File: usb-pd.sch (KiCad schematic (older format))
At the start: 32 parts, among them J12 12401598E4_2A, Q7 SQS401EN-T1_BE3, U18 STUSB4500QTR

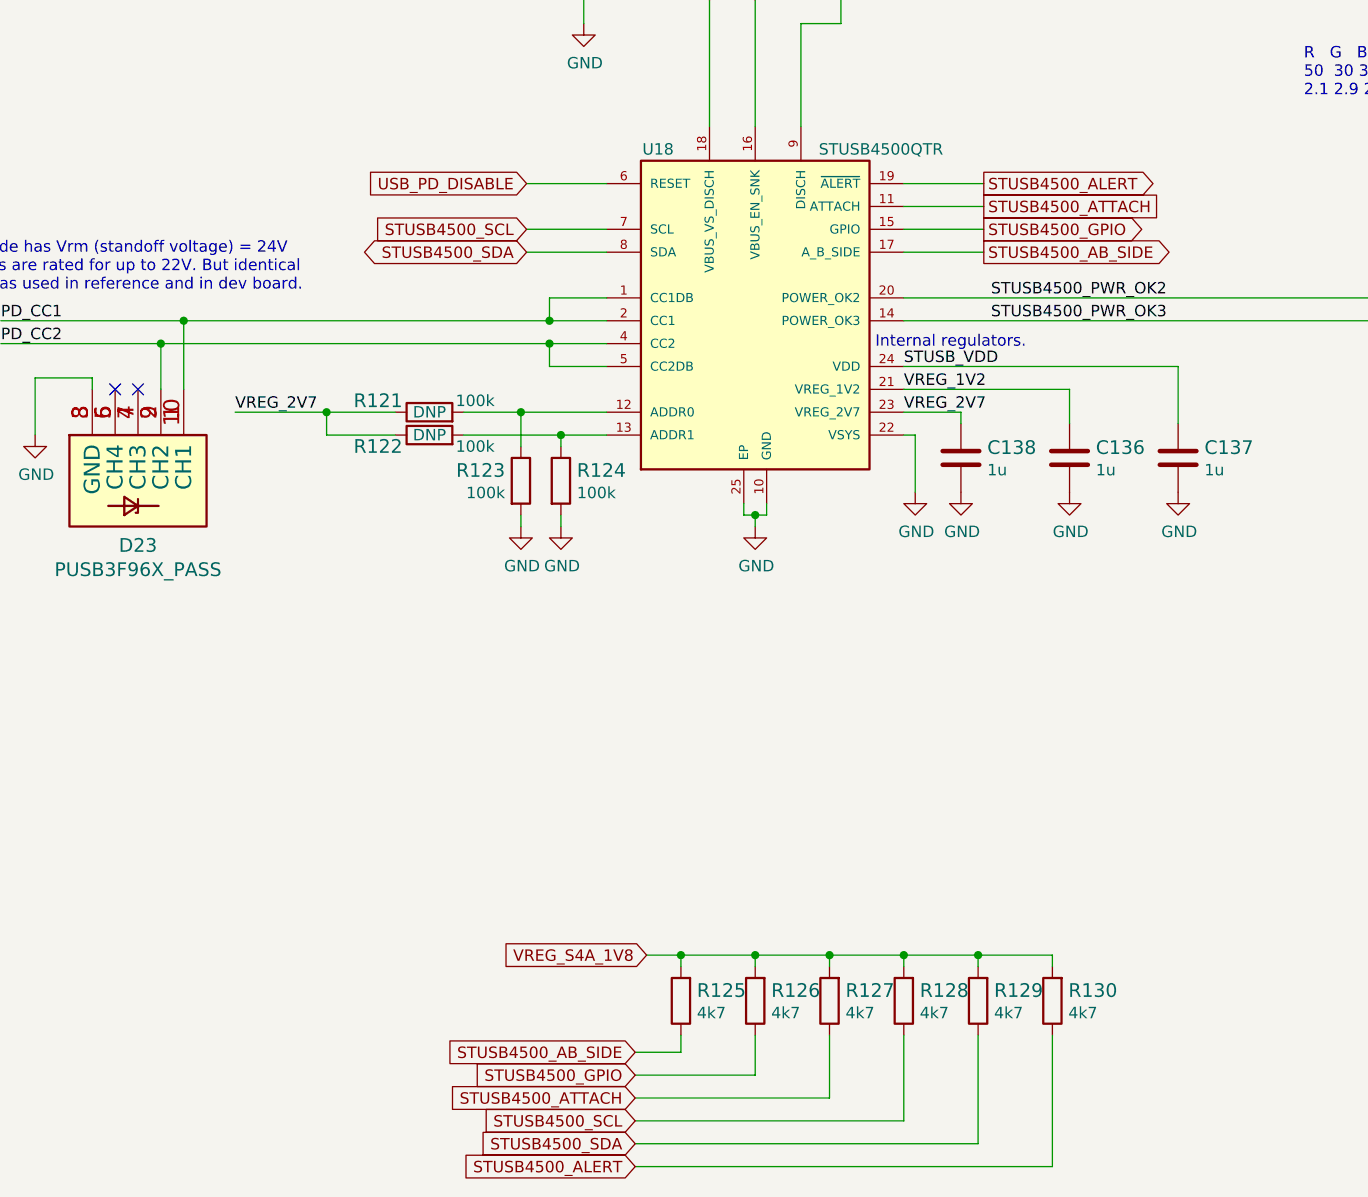
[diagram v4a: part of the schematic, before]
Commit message: Connect STUSB4500 signals to SoM
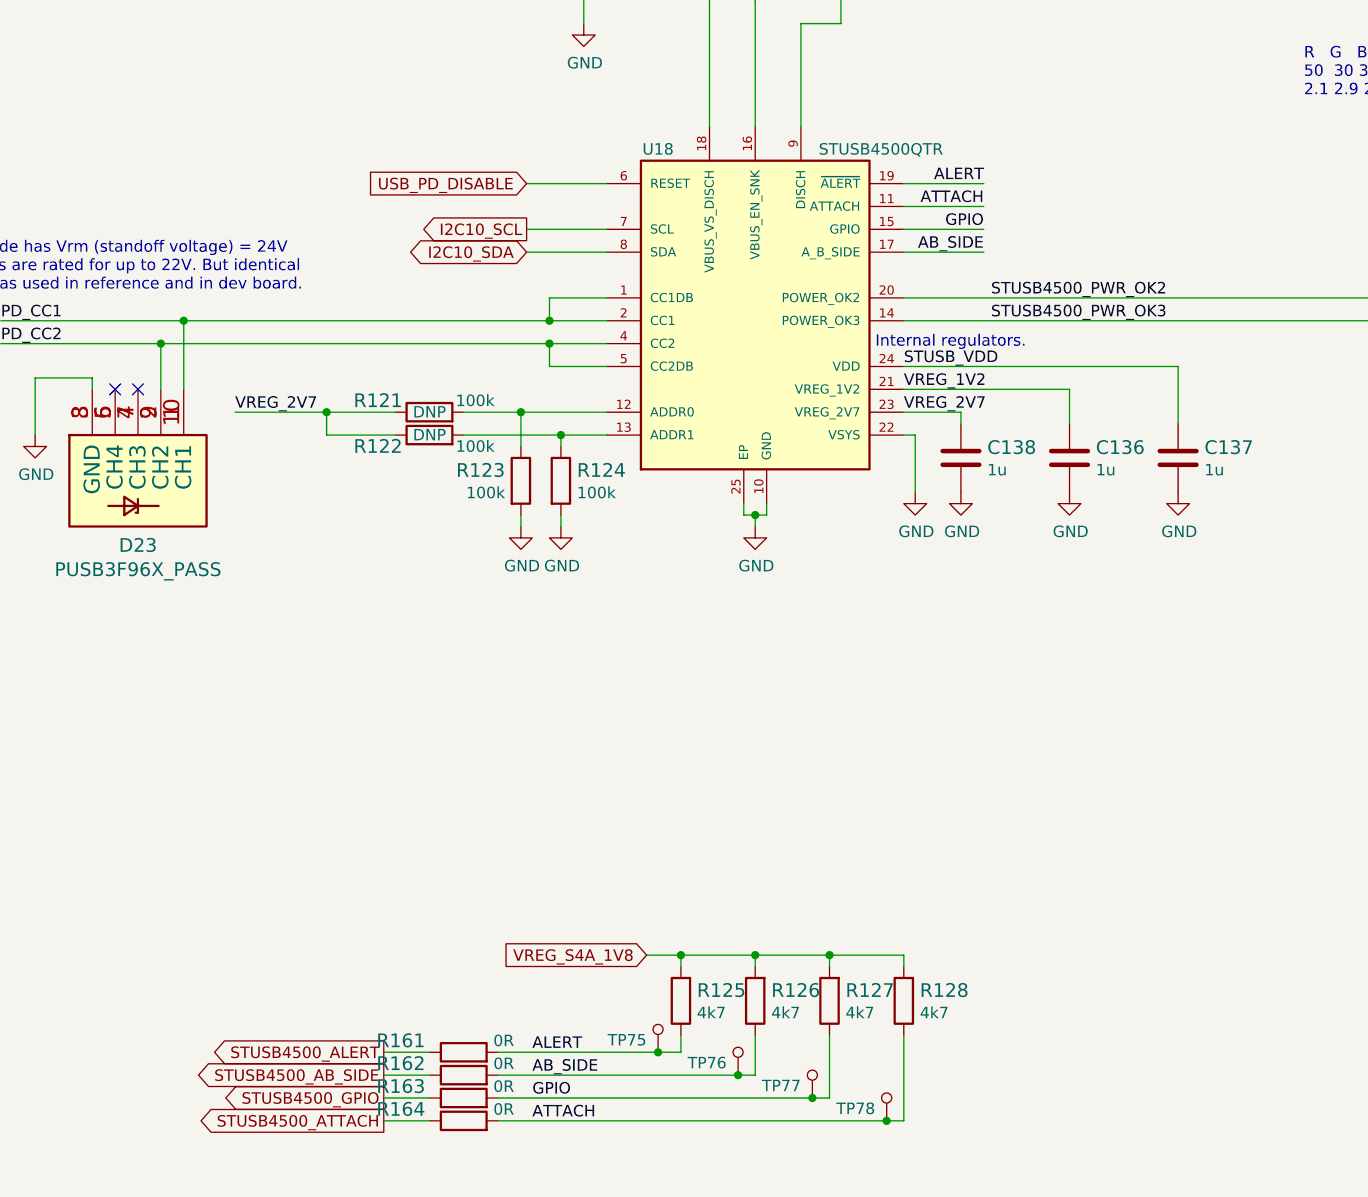
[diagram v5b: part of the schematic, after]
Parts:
- removed R129, R130: R_4k7_0402, sa800u-baseboard-hw-footprints:0402-res, symbol sa800u-baseboard-hw:R_4k7_0402
- added R161, R162, R163, R164: R_0R_0402, sa800u-baseboard-hw-footprints:0402-res, symbol sa800u-baseboard-hw:R_0R_0402
- added TP75, TP76, TP77, TP78: TP_SMD_0_75MM, sa800u-baseboard-hw-footprints:Testpoint_smd_0_75mm, symbol sa800u-baseboard-hw:TP_SMD_0_75MM
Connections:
- net STUSB4500_AB_SIDE: now also R162.1; no longer R125.1, U18.17 (A_B_SIDE)
- net STUSB4500_ALERT: now also R161.1; no longer U18.19 (~ALERT)
- net STUSB4500_ATTACH: now also R164.1; no longer R127.1, U18.11 (ATTACH)
- net STUSB4500_GPIO: now also R163.1; no longer R126.1, U18.15 (GPIO)
- net STUSB4500_SCL renamed ATTACH
- net ATTACH: now also U18.11 (ATTACH), R164.2, TP78.1; no longer U18.7 (SCL)
- net STUSB4500_SDA renamed I2C10_SDA
- new net AB_SIDE: R126.1, R162.2, TP76.1, U18.17 (A_B_SIDE)
- new net ALERT: R125.1, R161.2, TP75.1, U18.19 (~ALERT)
- new net GPIO: R127.1, R163.2, TP77.1, U18.15 (GPIO)
- new net I2C10_SCL: U18.7 (SCL)
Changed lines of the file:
@@
 	1    0    0    -1
 $EndComp
-Text GLabel 6350 4000 0    50   BiDi ~ 0
-STUSB4500_SDA
-Text GLabel 6350 3900 0    50   Input ~ 0
-STUSB4500_SCL
 Wire Wire Line
 	6350 3900 6700 3900
 Wire Wire Line
 	6350 4000 6700 4000
-Text GLabel 6825 7900 0    50   Input ~ 0
-STUSB4500_SDA
-Text GLabel 6825 7800 0    50   Input ~ 0
-STUSB4500_SCL
-Text GLabel 8350 3700 2    50   Output ~ 0
+Wire Wire Line
+	8000 3700 8350 3700
+Text GLabel 5725 7500 0    50   Output ~ 0
 STUSB4500_ALERT
 Wire Wire Line
-	8000 3700 8350 3700
-Text GLabel 6825 8000 0    50   Input ~ 0
-STUSB4500_ALERT
-Wire Wire Line
 	8000 3800 8350 3800
-Text GLabel 8350 3800 2    50   UnSpc ~ 0
+Wire Wire Line
+	8000 3900 8350 3900
+Wire Wire Line
+	8350 4000 8000 4000
+Text GLabel 5725 7800 0    50   Output ~ 0
 STUSB4500_ATTACH
-Text GLabel 8350 3900 2    50   Output ~ 0
+Text GLabel 5725 7700 0    50   Output ~ 0
 STUSB4500_GPIO
-Wire Wire Line
-	8000 3900 8350 3900
-Text GLabel 8350 4000 2    50   Output ~ 0
-STUSB4500_AB_SIDE
-Wire Wire Line
-	8350 4000 8000 4000
-Text GLabel 6825 7700 0    50   Input ~ 0
-STUSB4500_ATTACH
-Text GLabel 6825 7600 0    50   Input ~ 0
-STUSB4500_GPIO
-Text GLabel 6825 7500 0    50   Input ~ 0
+Text GLabel 5725 7600 0    50   Output ~ 0
 STUSB4500_AB_SIDE
 Wire Wire Line
@@
 	7025 7500 7025 7425
 Wire Wire Line
-	6825 7500 7025 7500
-Wire Wire Line
 	7350 7600 7350 7425
 Wire Wire Line
-	6825 7600 7350 7600
+	6225 7600 7275 7600
 Wire Wire Line
 	7675 7700 7675 7425
 Wire Wire Line
-	6825 7700 7675 7700
+	6225 7700 7600 7700
 $Comp
 L sa800u-baseboard-hw:R_4k7_0402 R128
@@
 	0    -1   -1   0
 $EndComp
-$Comp
-L sa800u-baseboard-hw:R_4k7_0402 R129
-U 1 1 62F55A6F
-P 8325 7275
-F 0 "R129" V 8370 7205 60  0000 R CNN
-F 1 "R_4k7_0402" H 8325 7125 60  0001 C CNN
-F 2 "sa800u-baseboard-hw-footprints:0402-res" H 8525 7475 60  0001 L CNN
-F 3 "" H 8325 7275 50  0001 C CNN
-F 4 "VISHAY" H 8525 7675 60  0001 L CNN "Manufacturer"
-F 5 "MCS04020C4701FE000" H 8525 7575 60  0001 L CNN "MPN"
-F 6 "4k7" V 8272 7205 50  0000 R CNN "Val"
-	1    8325 7275
-	0    -1   -1   0
-$EndComp
 Wire Wire Line
 	7675 7075 8000 7075
@@
 	8000 7075 8000 7125
 Wire Wire Line
-	8000 7075 8325 7075
-Wire Wire Line
-	8325 7075 8325 7125
-Connection ~ 8000 7075
-$Comp
-L sa800u-baseboard-hw:R_4k7_0402 R130
-U 1 1 62F5B4FE
-P 8650 7275
-F 0 "R130" V 8695 7205 60  0000 R CNN
-F 1 "R_4k7_0402" H 8650 7125 60  0001 C CNN
-F 2 "sa800u-baseboard-hw-footprints:0402-res" H 8850 7475 60  0001 L CNN
-F 3 "" H 8650 7275 50  0001 C CNN
-F 4 "VISHAY" H 8850 7675 60  0001 L CNN "Manufacturer"
-F 5 "MCS04020C4701FE000" H 8850 7575 60  0001 L CNN "MPN"
-F 6 "4k7" V 8597 7205 50  0000 R CNN "Val"
-	1    8650 7275
-	0    -1   -1   0
-$EndComp
-Wire Wire Line
-	8325 7075 8650 7075
-Wire Wire Line
-	8650 7075 8650 7125
-Wire Wire Line
 	8000 7800 8000 7425
 Wire Wire Line
-	6825 7800 8000 7800
-Wire Wire Line
-	8325 7900 8325 7425
-Wire Wire Line
-	6825 7900 8325 7900
-Wire Wire Line
-	8650 8000 8650 7425
-Wire Wire Line
-	6825 8000 8650 8000
+	6225 7800 7925 7800
 Connection ~ 7675 7075
-Connection ~ 8325 7075
 Wire Wire Line
 	7150 2900 7150 3450
@@
 Text Label 5075 4700 0    50   ~ 0
 VREG_2V7
+$Comp
+L sa800u-baseboard-hw:TP_SMD_0_75MM TP?
+U 1 1 620ECAFB
+P 6925 7400
+AR Path="/61B0DC30/620ECAFB" Ref="TP?"  Part="1"
+AR Path="/61DF77CE/620ECAFB" Ref="TP75"  Part="1"
+F 0 "TP75" H 6975 7447 50  0000 L CNN
+F 1 "TP_SMD_0_75MM" H 6925 7300 50  0001 C CNN
+F 2 "sa800u-baseboard-hw-footprints:Testpoint_smd_0_75mm" H 7125 7600 60  0001 L CNN
+F 3 "" H 7125 7700 60  0001 L CNN
+	1    6925 7400
+	-1   0    0    1
+$EndComp
+$Comp
+L sa800u-baseboard-hw:TP_SMD_0_75MM TP?
+U 1 1 6211F056
+P 7275 7500
+AR Path="/61B0DC30/6211F056" Ref="TP?"  Part="1"
+AR Path="/61DF77CE/6211F056" Ref="TP76"  Part="1"
+F 0 "TP76" H 7325 7547 50  0000 L CNN
+F 1 "TP_SMD_0_75MM" H 7275 7400 50  0001 C CNN
+F 2 "sa800u-baseboard-hw-footprints:Testpoint_smd_0_75mm" H 7475 7700 60  0001 L CNN
+F 3 "" H 7475 7800 60  0001 L CNN
+	1    7275 7500
+	-1   0    0    1
+$EndComp
+$Comp
+L sa800u-baseboard-hw:TP_SMD_0_75MM TP?
+U 1 1 62123DE3
+P 7600 7600
+AR Path="/61B0DC30/62123DE3" Ref="TP?"  Part="1"
+AR Path="/61DF77CE/62123DE3" Ref="TP77"  Part="1"
+F 0 "TP77" H 7650 7647 50  0000 L CNN
+F 1 "TP_SMD_0_75MM" H 7600 7500 50  0001 C CNN
+F 2 "sa800u-baseboard-hw-footprints:Testpoint_smd_0_75mm" H 7800 7800 60  0001 L CNN
+F 3 "" H 7800 7900 60  0001 L CNN
+	1    7600 7600
+	-1   0    0    1
+$EndComp
+$Comp
+L sa800u-baseboard-hw:TP_SMD_0_75MM TP?
+U 1 1 6212893D
+P 7925 7700
+AR Path="/61B0DC30/6212893D" Ref="TP?"  Part="1"
+AR Path="/61DF77CE/6212893D" Ref="TP78"  Part="1"
+F 0 "TP78" H 7975 7747 50  0000 L CNN
+F 1 "TP_SMD_0_75MM" H 7925 7600 50  0001 C CNN
+F 2 "sa800u-baseboard-hw-footprints:Testpoint_smd_0_75mm" H 8125 7900 60  0001 L CNN
+F 3 "" H 8125 8000 60  0001 L CNN
+	1    7925 7700
+	-1   0    0    1
+$EndComp
+Connection ~ 7925 7800
+Wire Wire Line
+	7925 7800 8000 7800
+Connection ~ 7600 7700
+Wire Wire Line
+	7600 7700 7675 7700
+Connection ~ 7275 7600
+Wire Wire Line
+	7275 7600 7350 7600
+Connection ~ 6925 7500
+Wire Wire Line
+	6925 7500 7025 7500
+Wire Wire Line
+	6225 7500 6925 7500
+$Comp
+L sa800u-baseboard-hw:R_0R_0402 R?
+U 1 1 62272ADE
+P 6075 7600
+AR Path="/61C01D88/62272ADE" Ref="R?"  Part="1"
+AR Path="/61DF77CE/62272ADE" Ref="R162"  Part="1"
+F 0 "R162" H 5800 7650 60  0000 C CNN
+F 1 "R_0R_0402" H 6075 7450 60  0001 C CNN
+F 2 "sa800u-baseboard-hw-footprints:0402-res" H 6275 7800 60  0001 L CNN
+F 3 "" H 6075 7600 50  0001 C CNN
+F 4 "PANASONIC" H 6275 8000 60  0001 L CNN "Manufacturer"
+F 5 "ERJ2GE0R00X" H 6275 7900 60  0001 L CNN "MPN"
+F 6 "0R" H 6250 7650 50  0000 C CNN "Val"
+	1    6075 7600
+	1    0    0    -1
+$EndComp
+$Comp
+L sa800u-baseboard-hw:R_0R_0402 R?
+U 1 1 6228B532
+P 6075 7500
+AR Path="/61C01D88/6228B532" Ref="R?"  Part="1"
+AR Path="/61DF77CE/6228B532" Ref="R161"  Part="1"
+F 0 "R161" H 5800 7550 60  0000 C CNN
+F 1 "R_0R_0402" H 6075 7350 60  0001 C CNN
+F 2 "sa800u-baseboard-hw-footprints:0402-res" H 6275 7700 60  0001 L CNN
+F 3 "" H 6075 7500 50  0001 C CNN
+F 4 "PANASONIC" H 6275 7900 60  0001 L CNN "Manufacturer"
+F 5 "ERJ2GE0R00X" H 6275 7800 60  0001 L CNN "MPN"
+F 6 "0R" H 6250 7550 50  0000 C CNN "Val"
+	1    6075 7500
+	1    0    0    -1
+$EndComp
+$Comp
+L sa800u-baseboard-hw:R_0R_0402 R?
+U 1 1 622914DD
+P 6075 7800
+AR Path="/61C01D88/622914DD" Ref="R?"  Part="1"
+AR Path="/61DF77CE/622914DD" Ref="R164"  Part="1"
+F 0 "R164" H 5800 7850 60  0000 C CNN
+F 1 "R_0R_0402" H 6075 7650 60  0001 C CNN
+F 2 "sa800u-baseboard-hw-footprints:0402-res" H 6275 8000 60  0001 L CNN
+F 3 "" H 6075 7800 50  0001 C CNN
+F 4 "PANASONIC" H 6275 8200 60  0001 L CNN "Manufacturer"
+F 5 "ERJ2GE0R00X" H 6275 8100 60  0001 L CNN "MPN"
+F 6 "0R" H 6250 7850 50  0000 C CNN "Val"
+	1    6075 7800
+	1    0    0    -1
+$EndComp
+$Comp
+L sa800u-baseboard-hw:R_0R_0402 R?
+U 1 1 622914E6
+P 6075 7700
+AR Path="/61C01D88/622914E6" Ref="R?"  Part="1"
+AR Path="/61DF77CE/622914E6" Ref="R163"  Part="1"
+F 0 "R163" H 5800 7750 60  0000 C CNN
+F 1 "R_0R_0402" H 6075 7550 60  0001 C CNN
+F 2 "sa800u-baseboard-hw-footprints:0402-res" H 6275 7900 60  0001 L CNN
+F 3 "" H 6075 7700 50  0001 C CNN
+F 4 "PANASONIC" H 6275 8100 60  0001 L CNN "Manufacturer"
+F 5 "ERJ2GE0R00X" H 6275 8000 60  0001 L CNN "MPN"
+F 6 "0R" H 6250 7750 50  0000 C CNN "Val"
+	1    6075 7700
+	1    0    0    -1
+$EndComp
+Wire Wire Line
+	5925 7500 5725 7500
+Wire Wire Line
+	5925 7600 5725 7600
+Wire Wire Line
+	5925 7700 5725 7700
+Wire Wire Line
+	5925 7800 5725 7800
+Text Label 6375 7500 0    50   ~ 0
+ALERT
+Text Label 6375 7600 0    50   ~ 0
+AB_SIDE
+Text Label 6375 7700 0    50   ~ 0
+GPIO
+Text Label 6375 7800 0    50   ~ 0
+ATTACH
+Text Label 8350 3700 2    50   ~ 0
+ALERT
+Text Label 8350 4000 2    50   ~ 0
+AB_SIDE
+Text Label 8350 3900 2    50   ~ 0
+GPIO
+Text Label 8350 3800 2    50   ~ 0
+ATTACH
+Text GLabel 6350 3900 0    50   Output ~ 0
+I2C10_SCL
+Text GLabel 6350 4000 0    50   BiDi ~ 0
+I2C10_SDA
 $EndSCHEMATC

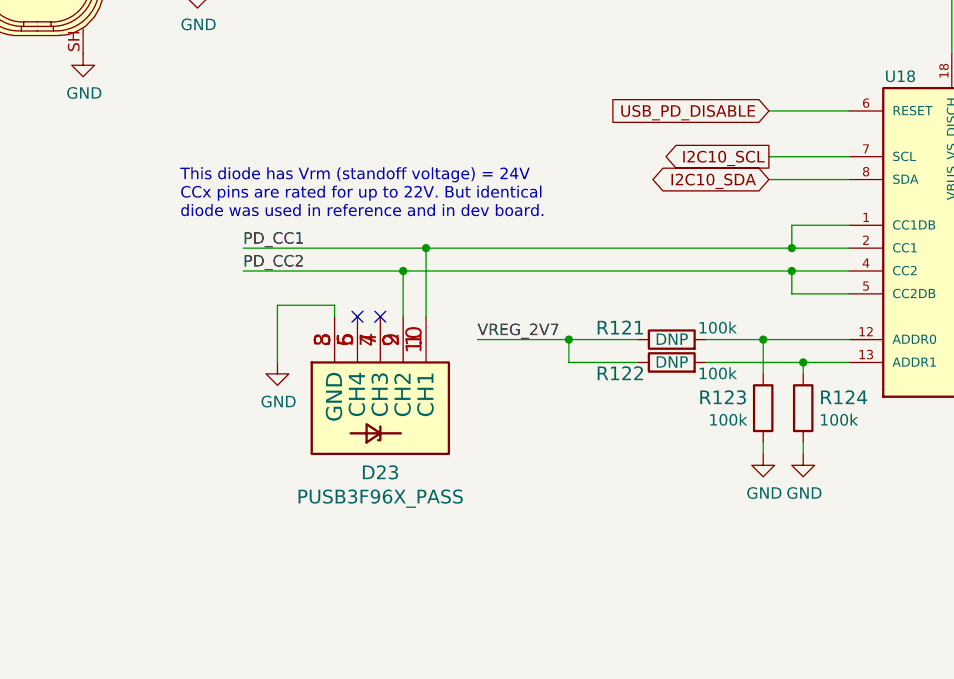
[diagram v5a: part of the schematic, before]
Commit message: Change USB-C PD CC TSV diode to 18V tolerant
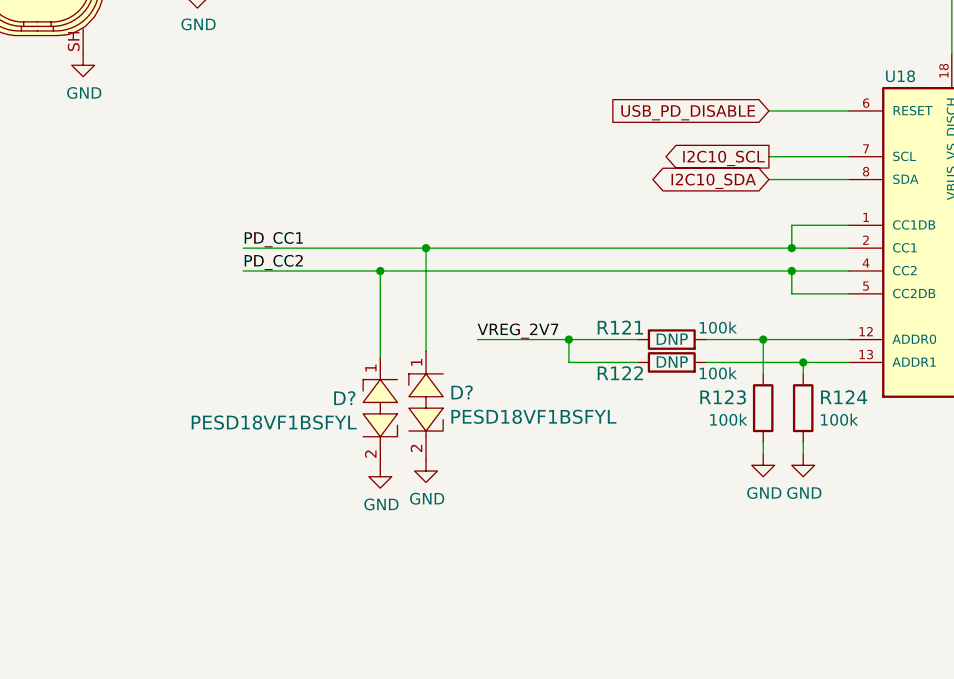
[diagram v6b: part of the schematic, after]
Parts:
- removed D23: PUSB3F96X_PASS, sa800u-baseboard-hw-footprints:PUSB3F96X, symbol sa800u-baseboard-hw:PUSB3F96X_PASS
- added D? (x2): PESD18VF1BSFYL, sa800u-baseboard-hw-footprints:RESC0603X26N, symbol sa800u-baseboard-hw:PESD18VF1BSFYL
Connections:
- net GND: now also D?.2, D?.2
- net PD_CC1: now also D?.1
- net PD_CC2: now also D?.1
- no-connect marks 16 -> 14
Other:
- note removed: "This diode has Vrm (standoff voltage) = 24V\nCCx pins are rated for up to 22V. But identical\ndiode was used in reference and in dev board."
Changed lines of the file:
@@
 Wire Wire Line
 	3650 2650 4350 2650
-$Comp
-L sa800u-baseboard-hw:GND #PWR0197
-U 1 1 61E7DBDA
-P 4200 4800
-F 0 "#PWR0197" H 4200 4550 50  0001 C CNN
-F 1 "GND" H 4205 4627 50  0000 C CNN
-F 2 "" H 4200 4800 50  0001 C CNN
-F 3 "" H 4200 4800 50  0001 C CNN
-	1    4200 4800
-	1    0    0    -1
-$EndComp
 Wire Wire Line
 	6450 4300 6450 4200
@@
 Wire Wire Line
 	6450 4400 6700 4400
-Text Notes 3775 4175 0    50   ~ 0
-This diode has Vrm (standoff voltage) = 24V\nCCx pins are rated for up to 22V. But identical\ndiode was used in reference and in dev board.
 $Comp
 L sa800u-baseboard-hw:C_1u_0402 C136
@@
 Text GLabel 10500 2925 0    50   Input ~ 0
 5V_SYS
-Text Notes 9750 3325 0    50   ~ 0
-R   G   B\n50  30 30 [mA]\n2.1 2.9 2.9 [V]
 Wire Wire Line
 	10500 2600 7725 2600
@@
 	1    0    0    -1
 $EndComp
-$Comp
-L sa800u-baseboard-hw:PUSB3F96X_PASS D?
-U 1 1 6298EA5C
-P 4650 4800
-AR Path="/6197686D/6298EA5C" Ref="D?"  Part="1"
-AR Path="/61A2F307/6298EA5C" Ref="D?"  Part="1"
-AR Path="/61DF77CE/6298EA5C" Ref="D23"  Part="1"
-F 0 "D23" V 5133 4800 60  0000 C CNN
-F 1 "PUSB3F96X_PASS" V 5239 4800 60  0000 C CNN
-F 2 "sa800u-baseboard-hw-footprints:PUSB3F96X" H 4850 4250 60  0001 C CNN
-F 3 "https://pl.mouser.com/datasheet/2/916/PUSB3F96-1600324.pdf" H 4650 4800 60  0001 C CNN
-F 4 "Nexperia" H 4850 4150 50  0001 C CNN "Manufacturer"
-F 5 "PUSB3F96X" H 4850 4150 50  0001 C CNN "MPN"
-	1    4650 4800
-	0    1    1    0
-$EndComp
-Wire Wire Line
-	4200 4550 4450 4550
-Wire Wire Line
-	4450 4550 4450 4600
-Wire Wire Line
-	4200 4550 4200 4800
-Connection ~ 4750 4400
-Wire Wire Line
-	4750 4400 6450 4400
-Wire Wire Line
-	4050 4400 4750 4400
-Wire Wire Line
-	4750 4400 4750 4600
-Wire Wire Line
-	4850 4300 4850 4600
-NoConn ~ 4550 4600
-NoConn ~ 4650 4600
+Wire Wire Line
+	4050 4400 4650 4400
+Wire Wire Line
+	4850 4300 4850 4750
 $Comp
 L sa800u-baseboard-hw:12401598E4_2A J12
@@
 Text GLabel 6350 4000 0    50   BiDi ~ 0
 I2C10_SDA
+$Comp
+L sa800u-baseboard-hw:GND #PWR?
+U 1 1 629F9470
+P 4850 5225
+F 0 "#PWR?" H 4850 4975 50  0001 C CNN
+F 1 "GND" H 4855 5052 50  0000 C CNN
+F 2 "" H 4850 5225 50  0001 C CNN
+F 3 "" H 4850 5225 50  0001 C CNN
+	1    4850 5225
+	1    0    0    -1
+$EndComp
+$Comp
+L sa800u-baseboard-hw:PESD18VF1BSFYL D?
+U 1 1 629F9478
+P 4850 4975
+F 0 "D?" V 4809 5078 60  0000 L CNN
+F 1 "PESD18VF1BSFYL" V 4915 5078 60  0000 L CNN
+F 2 "sa800u-baseboard-hw-footprints:RESC0603X26N" H 4850 4525 100 0001 L CNN
+F 3 "https://www.mouser.pl/datasheet/2/916/PESD18VF1BSF-1599696.pdf" H 5060 4825 100 0001 C CNN
+F 4 "nexperia" H 4850 4400 100 0001 L CNN "Manufacturer"
+F 5 "PESD18VF1BSFYL" H 4850 4650 100 0001 L CNN "MPN"
+	1    4850 4975
+	0    1    1    0
+$EndComp
+$Comp
+L sa800u-baseboard-hw:GND #PWR?
+U 1 1 62A0542C
+P 4650 5250
+F 0 "#PWR?" H 4650 5000 50  0001 C CNN
+F 1 "GND" H 4655 5077 50  0000 C CNN
+F 2 "" H 4650 5250 50  0001 C CNN
+F 3 "" H 4650 5250 50  0001 C CNN
+	1    4650 5250
+	1    0    0    -1
+$EndComp
+$Comp
+L sa800u-baseboard-hw:PESD18VF1BSFYL D?
+U 1 1 62A05434
+P 4650 5000
+F 0 "D?" V 4609 4897 60  0000 R CNN
+F 1 "PESD18VF1BSFYL" V 4715 4897 60  0000 R CNN
+F 2 "sa800u-baseboard-hw-footprints:RESC0603X26N" H 4650 4550 100 0001 L CNN
+F 3 "https://www.mouser.pl/datasheet/2/916/PESD18VF1BSF-1599696.pdf" H 4860 4850 100 0001 C CNN
+F 4 "nexperia" H 4650 4425 100 0001 L CNN "Manufacturer"
+F 5 "PESD18VF1BSFYL" H 4650 4675 100 0001 L CNN "MPN"
+	1    4650 5000
+	0    1    1    0
+$EndComp
+Wire Wire Line
+	4650 4775 4650 4400
+Connection ~ 4650 4400
+Wire Wire Line
+	4650 4400 6450 4400
+Text Notes 9750 3325 0    50   ~ 0
+R   G   B\n50  30 30 [mA]\n2.1 2.9 2.9 [V]
 $EndSCHEMATC
